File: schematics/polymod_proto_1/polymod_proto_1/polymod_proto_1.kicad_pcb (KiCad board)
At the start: 2 copper layers, 138 x 115 mm, 133 parts, among them J1 Conn_01x02_Male, J10 Conn_01x08_Male, J11 Conn_01x08_Male, J12 Conn_01x08_Male, J13 Conn_01x08_Male, J14 Conn_01x03_Male, J2 Conn_01x03_Male, J3 Conn_01x02_Male, J4 Barrel_Jack, J6 Conn_01x08_Male, J7 Conn_01x08_Male, J8 Conn_01x08_Male, J9 Conn_01x08_Male, SW1 SW_Push, SW2 SW_Push, SW3 SW_Push, SW4 SW_Push, U1 6N138, U10 74HC595, U11 74LS165, U12 74LS165, U13 74LS165, U2 74HC595, U3 74LS165, U4 4051, U5 74HC595, U6 74LS165, U7 4051, U8 74HC595, U9 74HC595

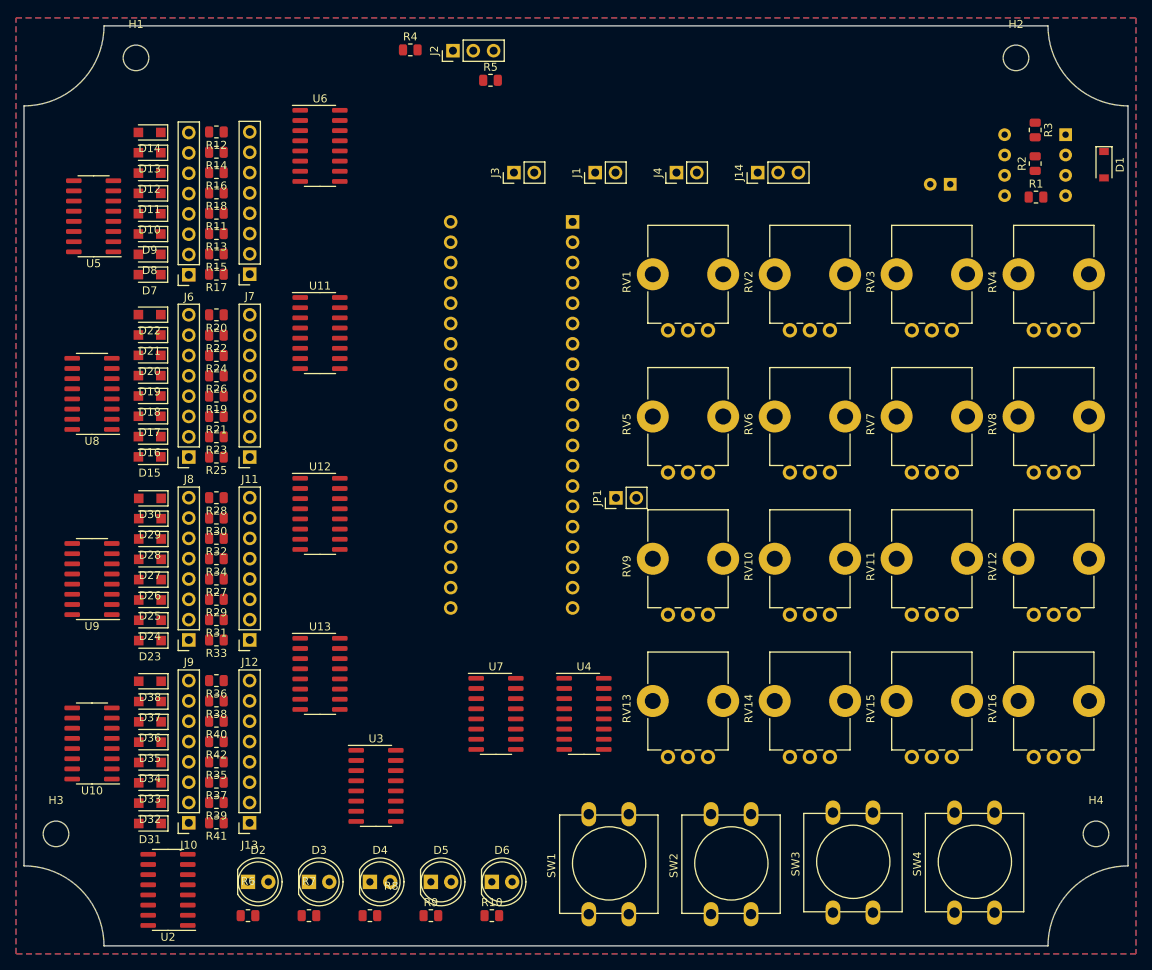
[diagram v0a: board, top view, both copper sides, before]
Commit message: really shouldn't be committing all these zip backups...
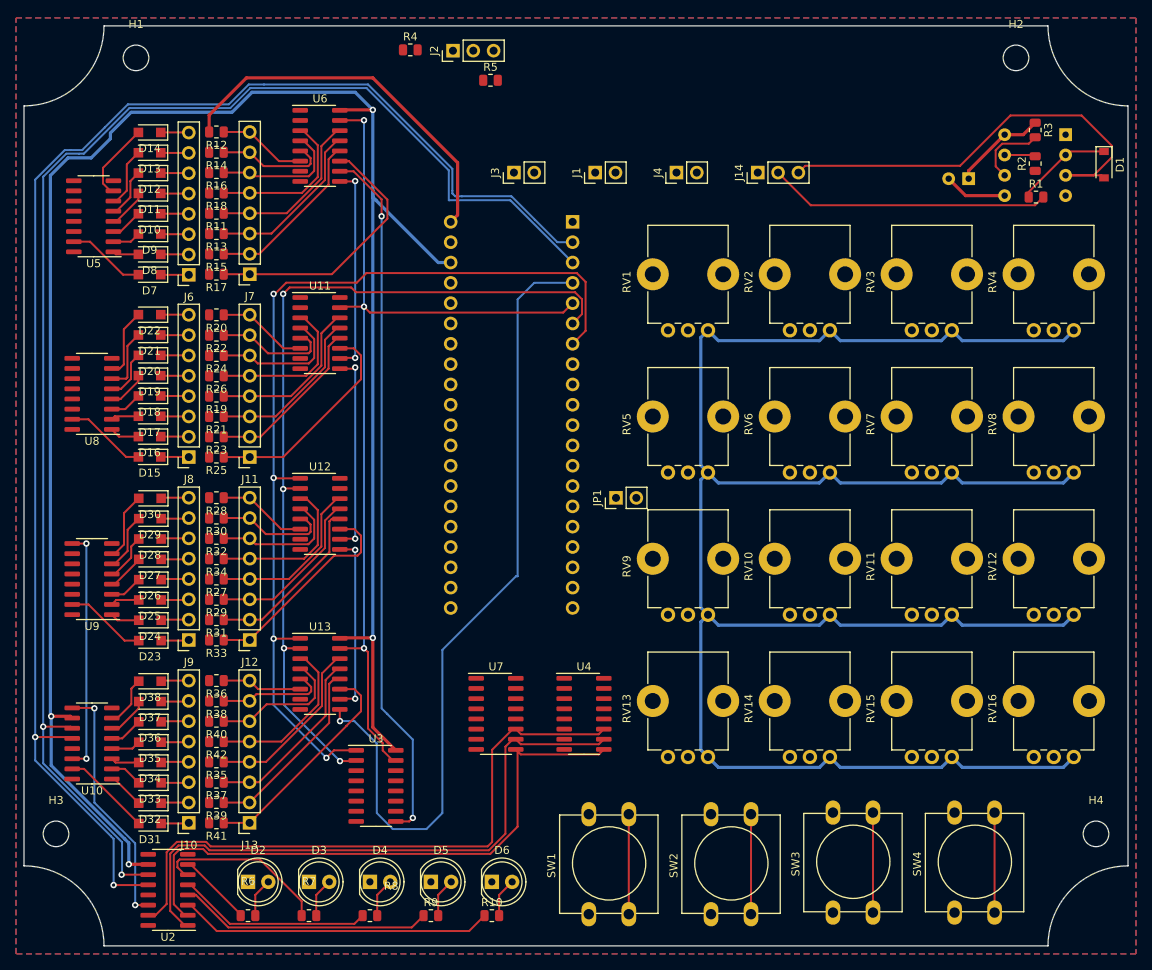
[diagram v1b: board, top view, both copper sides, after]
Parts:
- moved C1 2.40 mm to (199.1, 54.1)
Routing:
- net VCC: track 0.00 -> 507.9 mm, vias 0 -> 4
- net PATCHING_OUT_LATCH: track 0.00 -> 183.3 mm, vias 0 -> 2
- net PATCHING_OUT_CLOCK: track 0.00 -> 180.4 mm, vias 0 -> 2
- net PATCHING_IN_LOAD: track 0.00 -> 120.5 mm, vias 0 -> 4
- net PATCHING_IN_CE: track 0.00 -> 117.9 mm, vias 0 -> 3
- net PATCHING_IN_CLOCK: track 0.00 -> 109.4 mm, vias 0 -> 4
- net /PATCHING_IN_DATA: track 0.00 -> 101.7 mm, vias 0 -> 1
- net /UTIL_165: track 0.00 -> 87.9 mm, vias 0 -> 2
- net 4051_ADDRESS_A: track 0.00 -> 78.1 mm
- net 4051_ADDRESS_B: track 0.00 -> 77.6 mm
- net 4051_ADDRESS_C: track 0.00 -> 74.7 mm
- net /midi_in_tip: track 0.00 -> 56.8 mm
- net GND: track 0.00 -> 55.1 mm
- net Net-(R10-Pad1): track 0.00 -> 39.2 mm
- net /midi_in_ring: track 0.00 -> 35.3 mm
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
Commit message: mainly just ground routing now
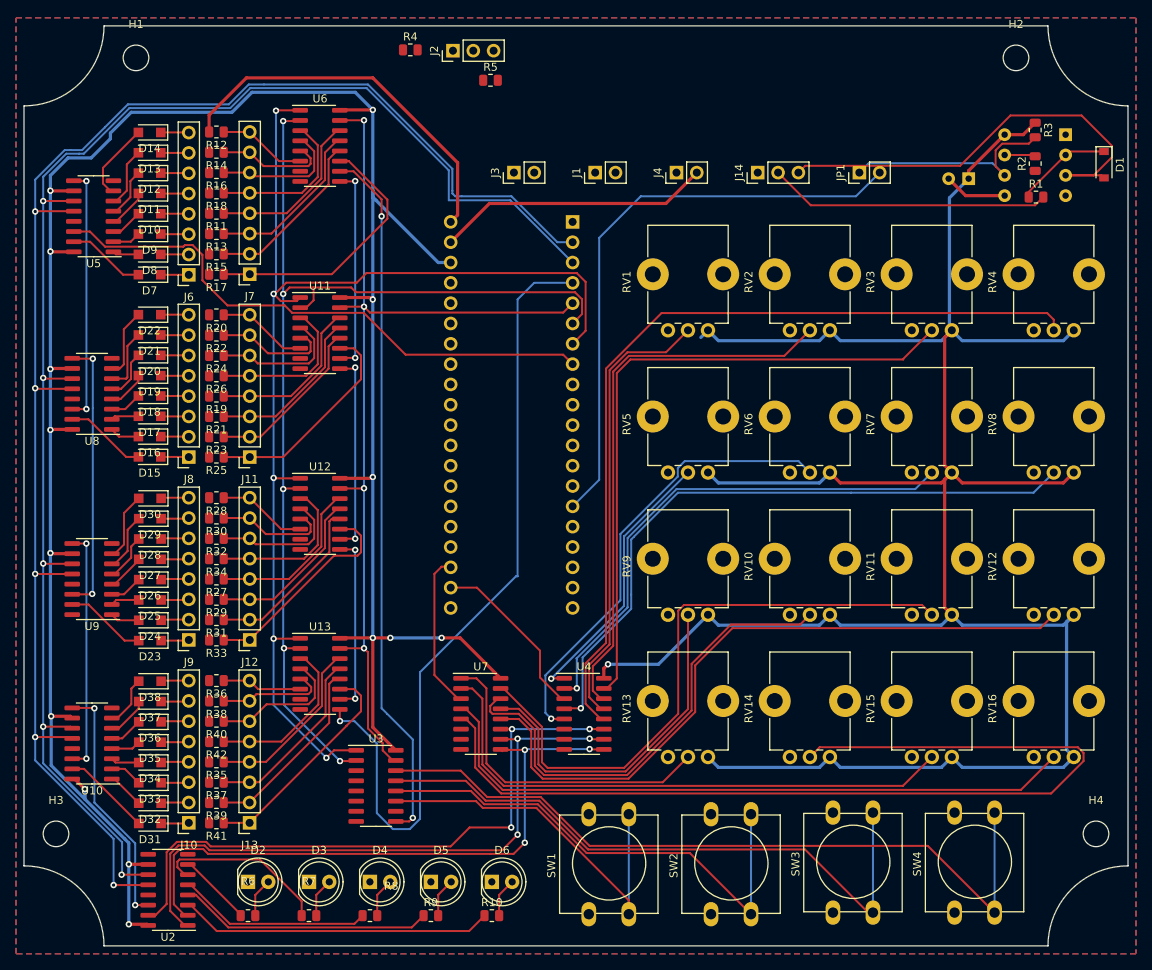
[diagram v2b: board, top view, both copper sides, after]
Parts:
- moved JP1 50.8 mm to (185.4, 53.3)
- moved U7 1.90 mm to (138.1, 121.0)
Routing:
- net Net-(RV14-Pad2): track 0.00 -> 122.3 mm
- net Net-(RV4-Pad2): track 0.00 -> 106.5 mm
- net VCC: track 507.9 -> 600.3 mm, vias 4 -> 16
- net Net-(RV12-Pad2): track 0.00 -> 86.8 mm
- net Net-(RV16-Pad2): track 0.00 -> 83.2 mm
- net Net-(SW4-Pad2): track 12.5 -> 94.7 mm
- net Net-(RV8-Pad2): track 0.00 -> 82.1 mm, vias 0 -> 1
- net Net-(RV3-Pad2): track 0.00 -> 82.0 mm
- net Net-(RV11-Pad2): track 0.00 -> 77.1 mm
- net /MIDI_IN: track 0.00 -> 73.4 mm
- net /PATCHING_OUT_DATA: track 0.00 -> 71.2 mm
- net Net-(RV15-Pad2): track 0.00 -> 70.2 mm
- net Net-(RV2-Pad2): track 0.00 -> 69.5 mm
- net Net-(SW3-Pad2): track 12.5 -> 79.0 mm
- net Net-(RV7-Pad2): track 0.00 -> 64.4 mm, vias 0 -> 1
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
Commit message: routed!
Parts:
- moved J1 50.3 mm to (142.7, 102.7)
- moved J3 44.3 mm to (142.6, 97.6)
- moved R11 0.36 mm to (105.4, 58.4)
- moved R12 0.36 mm to (105.4, 48.3)
- moved R13 0.36 mm to (105.4, 61.0)
- moved R14 0.36 mm to (105.4, 50.8)
- moved R15 0.36 mm to (105.4, 63.5)
- moved R16 0.36 mm to (105.4, 53.3)
- moved R17 0.36 mm to (105.4, 66.0)
- moved R18 0.36 mm to (105.4, 55.9)
- moved R19 0.36 mm to (105.4, 81.3)
- moved R20 0.36 mm to (105.4, 71.1)
- moved R21 0.36 mm to (105.4, 83.8)
- moved R22 0.36 mm to (105.4, 73.7)
- moved R23 0.36 mm to (105.4, 86.4)
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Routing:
- net GND: track 55.1 -> 257.9 mm, vias 0 -> 3
- net VCC: track 600.3 -> 674.9 mm, vias 16 -> 19
- net /MIDI_OUT: track 0.00 -> 57.0 mm, vias 0 -> 1
- net GNDA: track 0.00 -> 14.1 mm
- net /midi_out_ring: track 0.00 -> 7.89 mm
- net /audio_in_tip: track 0.00 -> 4.44 mm
- net /audio_out_tip: track 0.00 -> 4.39 mm
- net /midi_out_tip: track 0.00 -> 4.24 mm

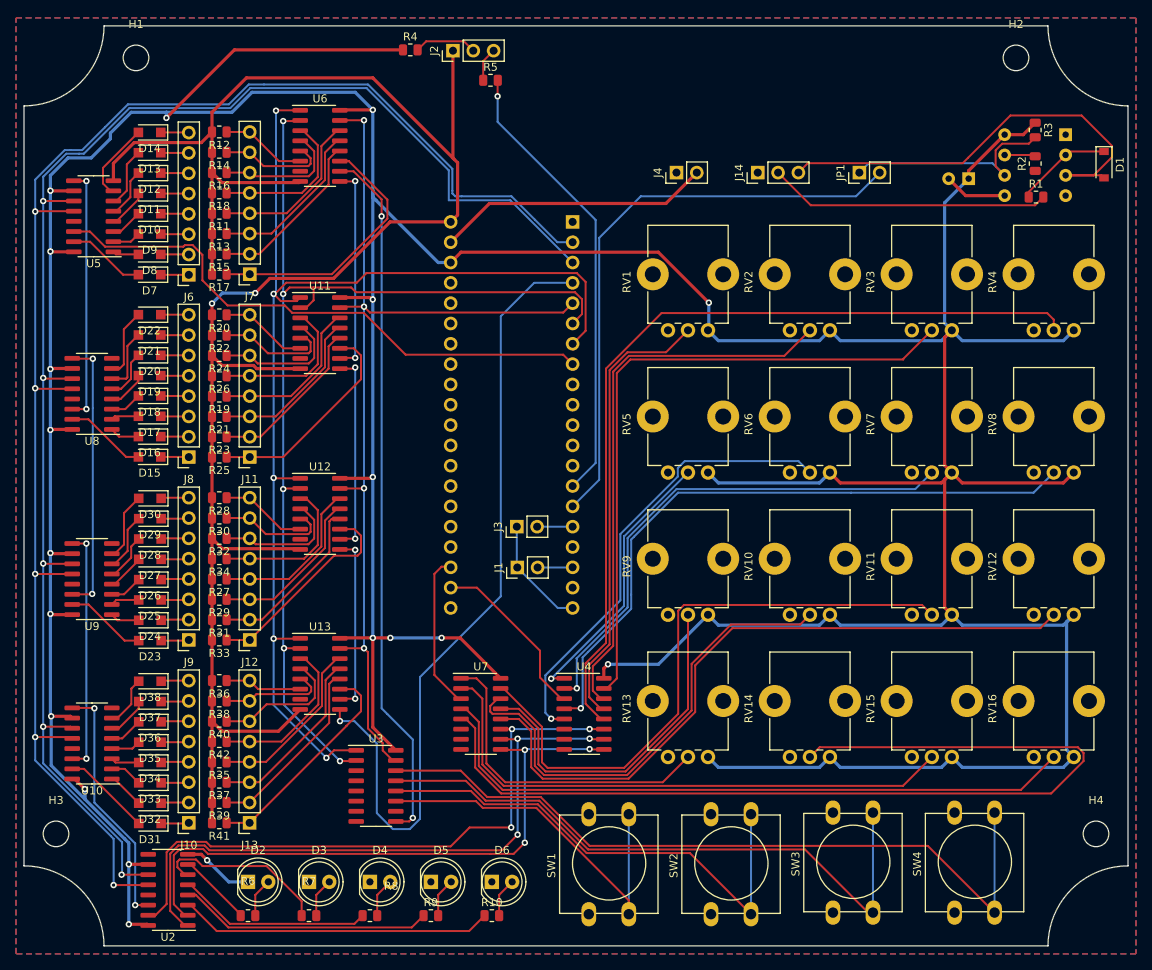
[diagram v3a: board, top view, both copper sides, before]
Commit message: no drc warnings
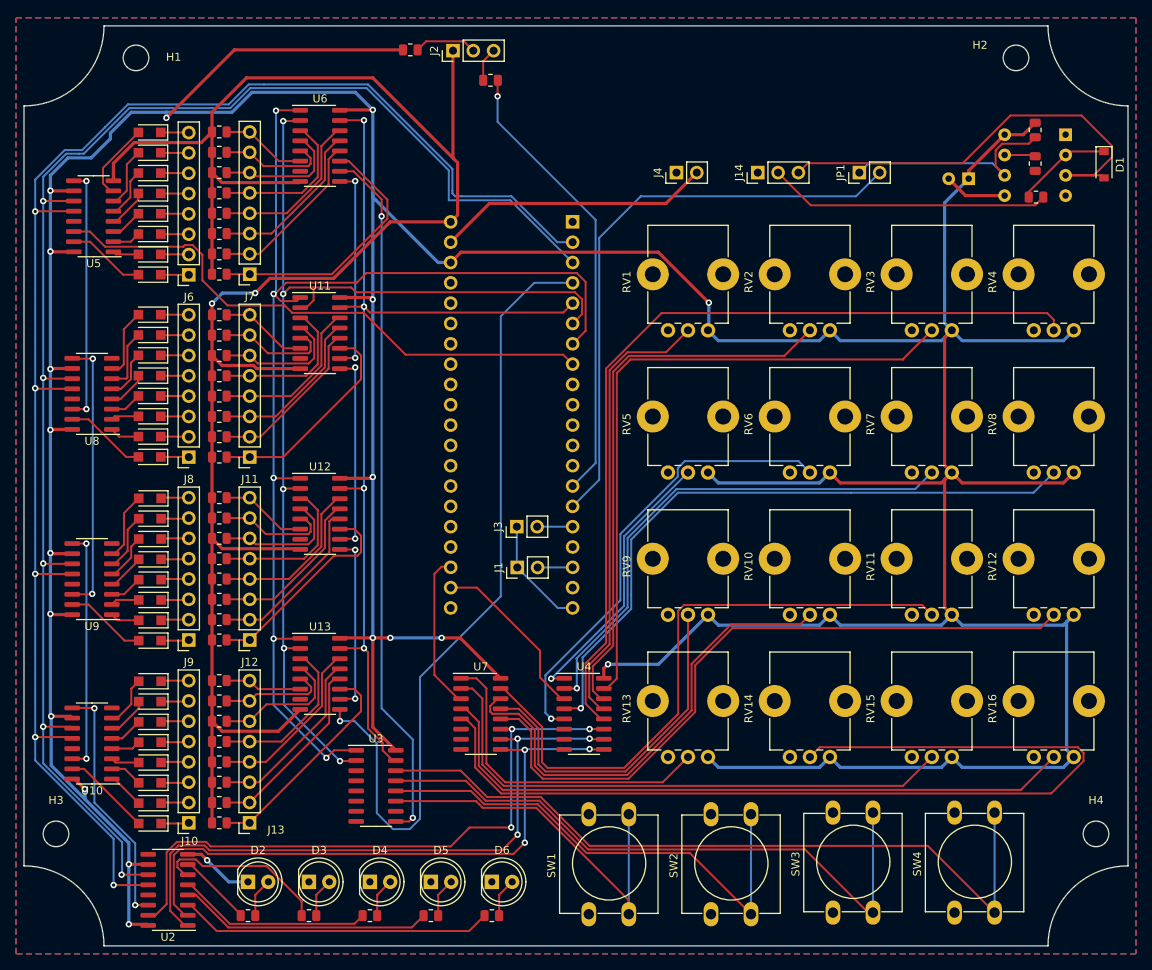
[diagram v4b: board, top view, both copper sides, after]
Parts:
- D10, D11, D12, D13, D14, D15, D16, D17, D18, D19, D20, D21, D22, D23, D24, D25, D26, D27, D28, D29, D30, D31, D32, D33, D34, D35, D36, D37, D38, D7, D8, D9: footprint Diode_SMD:Nexperia_CFP3_SOD-123W -> polymodcustom:Nexperia_CFP3_SOD-123W
- R1, R10, R11, R12, R13, R14, R15, R16, R17, R18, R19, R2, R20, R21, R22, R23, R24, R25, R26, R27, R28, R29, R3, R30, R31, R32, R33, R34, R35, R36, R37, R38, R39, R4, R40, R41, R42, R5, R6, R7, R8, R9: footprint Resistor_SMD:R_0805_2012Metric -> polymodcustom:R_0805_2012Metric
- SW1, SW2, SW3, SW4: footprint Button_Switch_THT:SW_PUSH-12mm -> polymodcustom:SW_PUSH-12mm

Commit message: added helpful notes
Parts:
- RV1, RV10, RV11, RV12, RV13, RV14, RV15, RV16, RV2, RV3, RV4, RV5, RV6, RV7, RV8, RV9: footprint Potentiometer_THT:Potentiometer_Alps_RK09K_Single_Vertical -> polymodcustom:Potentiometer_Alps_RK09K_Single_Vertical
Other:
- board text added: "- +"
- board text added: "- + Audio out"
- board text added: "Audio in - +"
- board text added: "MIDI in"
- board text added: "MIDI jumper"
- board text added: "MIDI out"
- board text added: "Power in"
- board text added: "S R T"
- board text added: "USB this end"

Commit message: maybe ready for fabrication!
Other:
- board text added: "Polyphonic semi-modular synthesizer Bradshaw Instruments (prototype) For 1590XX case July 2022"
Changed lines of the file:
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@@
     )
   )
+  (gr_line (start 142.7 43) (end 142.7 47) (layer "F.SilkS") (width 0.2))
+  (gr_circle (center 149.1 43) (end 151.1 43) (layer "F.SilkS") (width 0.2) (fill none))
+  (gr_line (start 151.9 41) (end 153.9 45) (layer "F.SilkS") (width 0.2))
+  (gr_circle (center 165.5 43) (end 167.5 43) (layer "F.SilkS") (width 0.2) (fill none))
+  (gr_line (start 153.9 45) (end 155.9 41) (layer "F.SilkS") (width 0.2))
+  (gr_line (start 153.9 45) (end 152.9 47) (layer "F.SilkS") (width 0.2))
+  (gr_line (start 153.9 45) (end 153.9 45) (layer "F.SilkS") (width 0.2))
+  (gr_circle (center 161.1 43) (end 163.1 43) (layer "F.SilkS") (width 0.2) (fill none))
+  (gr_line (start 167.5 43) (end 167.5 39) (layer "F.SilkS") (width 0.2))
+  (gr_line (start 154.7 45) (end 156.7 41) (layer "F.SilkS") (width 0.2))
+  (gr_line (start 151.5 45) (end 151.5 39) (layer "F.SilkS") (width 0.2))
+  (gr_circle (center 144.7 43) (end 146.7 43) (layer "F.SilkS") (width 0.2) (fill none))
+  (gr_line (start 158.7 41) (end 158.7 45) (layer "F.SilkS") (width 0.2))
+  (gr_line (start 156.7 45) (end 158.7 41) (layer "F.SilkS") (width 0.2))
+  (gr_line (start 156.7 41) (end 156.7 45) (layer "F.SilkS") (width 0.2))
   (gr_circle (center 164 43) (end 171 43) (layer "Dwgs.User") (width 0.2) (fill none))
   (gr_rect (start 77.5 32) (end 222.5 153) (layer "Dwgs.User") (width 0.15) (fill none))
@@
   (gr_text "MIDI out" (at 129.4 40.8) (layer "F.SilkS")
     (effects (font (size 1 1) (thickness 0.15)))
+  )
+  (gr_text "Polyphonic semi-modular synthesizer\nBradshaw Instruments (prototype)\nFor 1590XX case\nJuly 2022" (at 170.3 42) (layer "F.SilkS")
+    (effects (font (size 1 1) (thickness 0.2)) (justify left))
   )
   (gr_text "Power in" (at 163.8 51) (layer "F.SilkS")
@@
     )
   )
+  (group "" (id 67c5ed30-e4cc-4dcb-a867-ba0e95af4677)
+    (members
+      07b6b924-5cba-4166-99b0-badd2a0b44e1
+      10f3dfcf-9db2-4e9a-a434-d2de041151c4
+      1943da9f-d525-468f-bf0c-d83f83174a13
+      36514ea4-2c19-46c7-8a61-27202f0e011c
+      3809de13-4a90-4b1b-938c-120c43780965
+      38efeb53-4219-4d99-b1d1-0a3856681a78
+      538e4811-133d-4ccd-a738-a0d0cd4d1d5e
+      64205efa-47da-42bd-bff0-4d8c92a912cf
+      6d03d44b-d1b0-4f64-aef9-17f862c08336
+      89003258-54a3-4ec2-adbc-e25c47830bcf
+      8f84be1c-2e8a-427d-8482-a9872a7e37ff
+      953f9b16-b3a3-4d81-a150-48a8154877a9
+      b59ee653-ae13-4c29-bde1-52150c1f47b0
+      c727d1ef-a313-482f-8d94-00f89ce488af
+      fb4c815c-f261-421d-9723-e6ffdb5464e1
+    )
+  )
